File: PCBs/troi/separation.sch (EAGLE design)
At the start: 4 parts

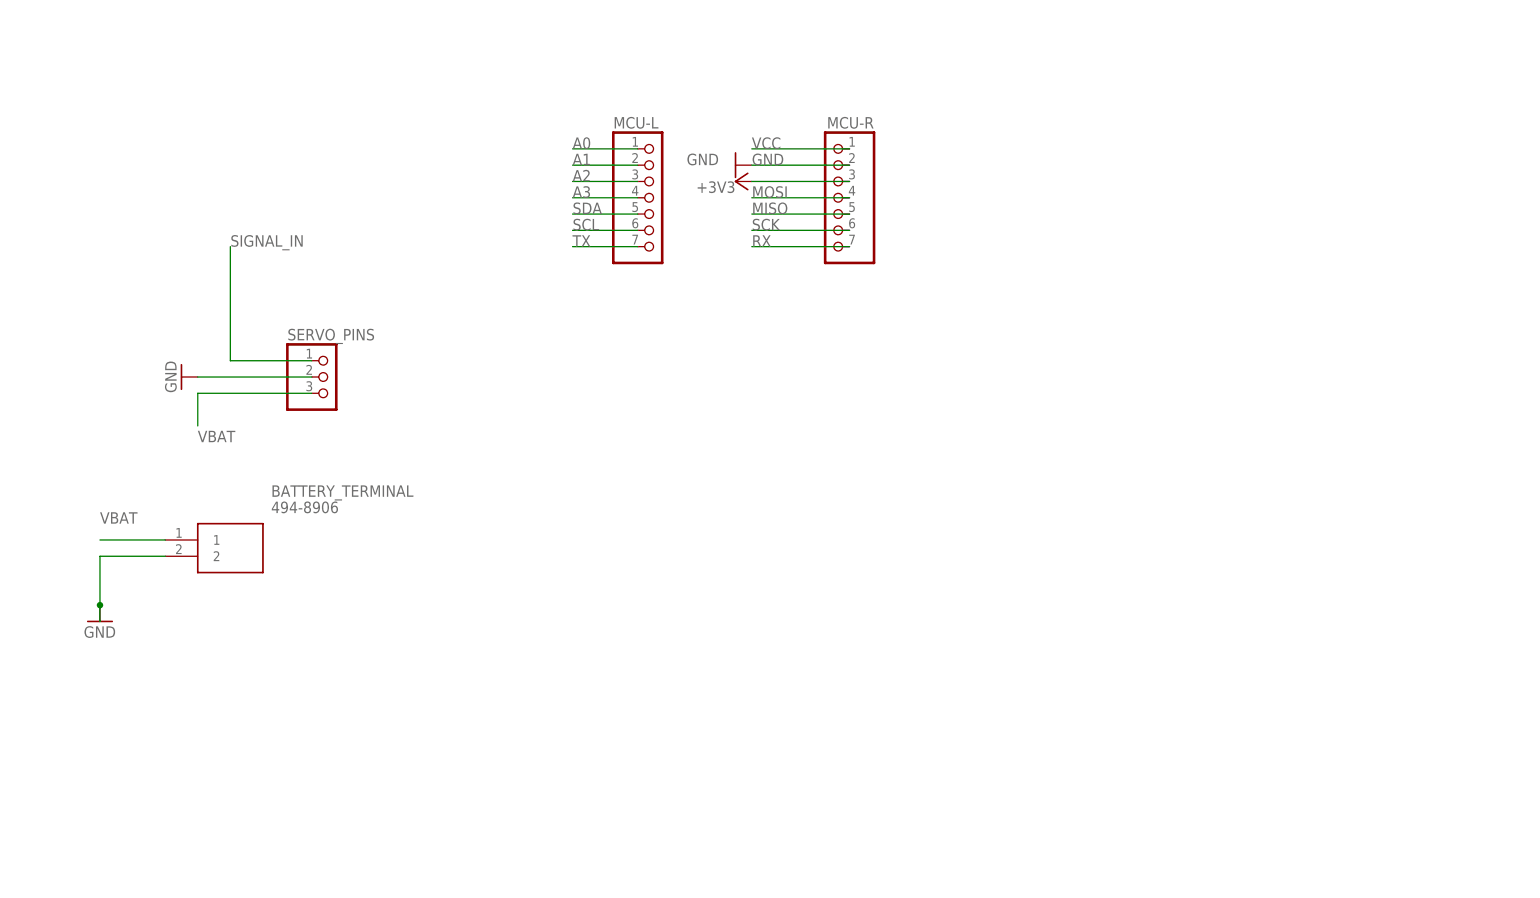
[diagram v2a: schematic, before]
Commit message: added mosfet transistor
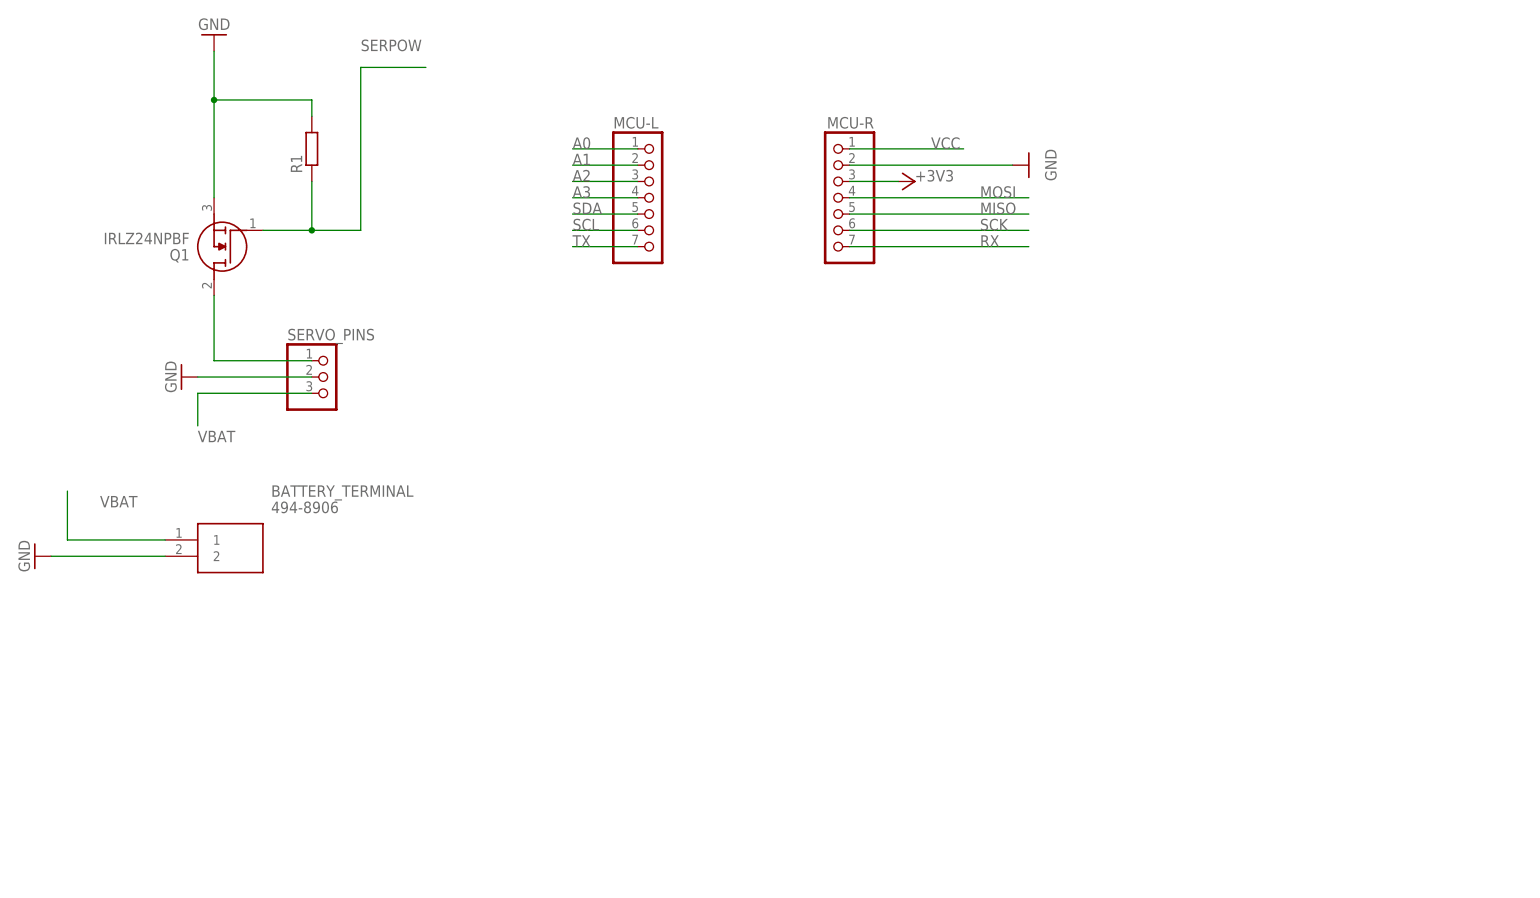
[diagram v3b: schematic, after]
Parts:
- added Q1: IRLZ24NPBF, SamacSys_Parts:IRLZ24NPBF
- added R1: (no value), rcl:R-EU_0204/7
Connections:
- removed net SIGNAL_IN: SERVO_PINS.1
- new net N$1: Q1.D, SERVO_PINS.1
- new net SERPOW: Q1.G, R1.1
- net GND: now also Q1.S, R1.2
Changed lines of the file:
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@@
 <part name="BATTERY_TERMINAL" library="494-8906" deviceset="494-8906" device=""/>
 <part name="GND3" library="supply1" library_urn="urn:adsk.eagle:library:371" deviceset="GND" device=""/>
+<part name="Q1" library="SamacSys_Parts" deviceset="IRLZ24NPBF" device=""/>
+<part name="GND4" library="supply1" library_urn="urn:adsk.eagle:library:371" deviceset="GND" device=""/>
+<part name="R1" library="rcl" library_urn="urn:adsk.eagle:library:334" deviceset="R-EU_" device="0204/7" package3d_urn="urn:adsk.eagle:package:23498/2"/>
 </parts>
 <sheets>
@@
 <attribute name="VALUE" x="115.57" y="68.58" size="1.778" layer="96" rot="MR0"/>
 </instance>
-<instance part="+3V1" gate="G$1" x="93.98" y="83.82" smashed="yes" rot="R90">
-<attribute name="VALUE" x="93.98" y="83.82" size="1.778" layer="96" rot="R180"/>
-</instance>
-<instance part="GND1" gate="1" x="93.98" y="86.36" smashed="yes" rot="R270">
-<attribute name="VALUE" x="86.36" y="86.36" size="1.778" layer="96"/>
+<instance part="+3V1" gate="G$1" x="121.92" y="83.82" smashed="yes" rot="R270">
+<attribute name="VALUE" x="121.92" y="83.82" size="1.778" layer="96"/>
+</instance>
+<instance part="GND1" gate="1" x="139.7" y="86.36" smashed="yes" rot="R90">
+<attribute name="VALUE" x="142.24" y="88.9" size="1.778" layer="96" rot="R270"/>
 </instance>
 <instance part="SERVO_PINS" gate="A" x="30.48" y="53.34" smashed="yes">
@@
 <attribute name="VALUE" x="21.59" y="33.02" size="1.778" layer="96" align="center-left"/>
 </instance>
-<instance part="GND3" gate="1" x="-5.08" y="15.24" smashed="yes">
-<attribute name="VALUE" x="-7.62" y="12.7" size="1.778" layer="96"/>
+<instance part="GND3" gate="1" x="-15.24" y="25.4" smashed="yes" rot="R270">
+<attribute name="VALUE" x="-17.78" y="27.94" size="1.778" layer="96" rot="R270"/>
+</instance>
+<instance part="Q1" gate="G$1" x="20.32" y="76.2" smashed="yes" rot="R180">
+<attribute name="NAME" x="8.89" y="72.39" size="1.778" layer="95" rot="R180" align="center-left"/>
+<attribute name="VALUE" x="8.89" y="74.93" size="1.778" layer="96" rot="R180" align="center-left"/>
+</instance>
+<instance part="GND4" gate="1" x="12.7" y="106.68" smashed="yes" rot="R180">
+<attribute name="VALUE" x="15.24" y="109.22" size="1.778" layer="96" rot="R180"/>
+</instance>
+<instance part="R1" gate="G$1" x="27.94" y="88.9" smashed="yes" rot="R90">
+<attribute name="NAME" x="26.4414" y="85.09" size="1.778" layer="95" rot="R90"/>
+<attribute name="VALUE" x="31.242" y="85.09" size="1.778" layer="96" rot="R90"/>
 </instance>
 </instances>
@@
 <segment>
 <pinref part="MCU-R" gate="A" pin="1"/>
-<wire x1="111.76" y1="88.9" x2="96.52" y2="88.9" width="0.1524" layer="91"/>
-<label x="96.52" y="88.9" size="1.778" layer="95"/>
+<wire x1="111.76" y1="88.9" x2="129.54" y2="88.9" width="0.1524" layer="91"/>
+<label x="124.46" y="88.9" size="1.778" layer="95"/>
 </segment>
 </net>
@@
 <segment>
 <pinref part="MCU-R" gate="A" pin="2"/>
-<wire x1="111.76" y1="86.36" x2="96.52" y2="86.36" width="0.1524" layer="91"/>
-<label x="96.52" y="86.36" size="1.778" layer="95"/>
+<wire x1="111.76" y1="86.36" x2="137.16" y2="86.36" width="0.1524" layer="91"/>
 <pinref part="GND1" gate="1" pin="GND"/>
 </segment>
@@
 <segment>
 <pinref part="BATTERY_TERMINAL" gate="G$1" pin="2"/>
-<wire x1="5.08" y1="25.4" x2="-5.08" y2="25.4" width="0.1524" layer="91"/>
-<wire x1="-5.08" y1="25.4" x2="-5.08" y2="17.78" width="0.1524" layer="91"/>
 <pinref part="GND3" gate="1" pin="GND"/>
-<wire x1="-5.08" y1="17.78" x2="-5.08" y2="15.24" width="0.1524" layer="91"/>
-<junction x="-5.08" y="17.78"/>
+<wire x1="5.08" y1="25.4" x2="-12.7" y2="25.4" width="0.1524" layer="91"/>
+</segment>
+<segment>
+<pinref part="Q1" gate="G$1" pin="S"/>
+<wire x1="12.7" y1="81.28" x2="12.7" y2="96.52" width="0.1524" layer="91"/>
+<wire x1="12.7" y1="96.52" x2="12.7" y2="104.14" width="0.1524" layer="91"/>
+<pinref part="GND4" gate="1" pin="GND"/>
+<pinref part="R1" gate="G$1" pin="2"/>
+<wire x1="27.94" y1="93.98" x2="27.94" y2="96.52" width="0.1524" layer="91"/>
+<wire x1="27.94" y1="96.52" x2="12.7" y2="96.52" width="0.1524" layer="91"/>
+<junction x="12.7" y="96.52"/>
 </segment>
 </net>
@@
 <segment>
 <pinref part="MCU-R" gate="A" pin="3"/>
-<wire x1="111.76" y1="83.82" x2="96.52" y2="83.82" width="0.1524" layer="91"/>
+<wire x1="111.76" y1="83.82" x2="119.38" y2="83.82" width="0.1524" layer="91"/>
 <pinref part="+3V1" gate="G$1" pin="+3V3"/>
 </segment>
@@
 <segment>
 <pinref part="MCU-R" gate="A" pin="4"/>
-<wire x1="111.76" y1="81.28" x2="96.52" y2="81.28" width="0.1524" layer="91"/>
-<label x="96.52" y="81.28" size="1.778" layer="95"/>
+<wire x1="111.76" y1="81.28" x2="139.7" y2="81.28" width="0.1524" layer="91"/>
+<label x="132.08" y="81.28" size="1.778" layer="95"/>
 </segment>
 </net>
@@
 <segment>
 <pinref part="MCU-R" gate="A" pin="5"/>
-<wire x1="111.76" y1="78.74" x2="96.52" y2="78.74" width="0.1524" layer="91"/>
-<label x="96.52" y="78.74" size="1.778" layer="95"/>
+<wire x1="111.76" y1="78.74" x2="139.7" y2="78.74" width="0.1524" layer="91"/>
+<label x="132.08" y="78.74" size="1.778" layer="95"/>
 </segment>
 </net>
@@
 <segment>
 <pinref part="MCU-R" gate="A" pin="6"/>
-<wire x1="111.76" y1="76.2" x2="96.52" y2="76.2" width="0.1524" layer="91"/>
-<label x="96.52" y="76.2" size="1.778" layer="95"/>
+<wire x1="111.76" y1="76.2" x2="139.7" y2="76.2" width="0.1524" layer="91"/>
+<label x="132.08" y="76.2" size="1.778" layer="95"/>
 </segment>
 </net>
@@
 <segment>
 <pinref part="MCU-R" gate="A" pin="7"/>
-<wire x1="111.76" y1="73.66" x2="96.52" y2="73.66" width="0.1524" layer="91"/>
-<label x="96.52" y="73.66" size="1.778" layer="95"/>
-</segment>
-</net>
-<net name="SIGNAL_IN" class="0">
-<segment>
-<pinref part="SERVO_PINS" gate="A" pin="1"/>
-<wire x1="27.94" y1="55.88" x2="15.24" y2="55.88" width="0.1524" layer="91"/>
-<wire x1="15.24" y1="55.88" x2="15.24" y2="73.66" width="0.1524" layer="91"/>
-<label x="15.24" y="73.66" size="1.778" layer="95"/>
+<wire x1="111.76" y1="73.66" x2="139.7" y2="73.66" width="0.1524" layer="91"/>
+<label x="132.08" y="73.66" size="1.778" layer="95"/>
 </segment>
 </net>
@@
 <segment>
 <pinref part="BATTERY_TERMINAL" gate="G$1" pin="1"/>
-<wire x1="5.08" y1="27.94" x2="-5.08" y2="27.94" width="0.1524" layer="91"/>
-<label x="-5.08" y="30.48" size="1.778" layer="95"/>
+<wire x1="5.08" y1="27.94" x2="-10.16" y2="27.94" width="0.1524" layer="91"/>
+<label x="-5.08" y="33.02" size="1.778" layer="95"/>
+<wire x1="-10.16" y1="27.94" x2="-10.16" y2="35.56" width="0.1524" layer="91"/>
+</segment>
+</net>
+<net name="N$1" class="0">
+<segment>
+<pinref part="SERVO_PINS" gate="A" pin="1"/>
+<wire x1="27.94" y1="55.88" x2="12.7" y2="55.88" width="0.1524" layer="91"/>
+<pinref part="Q1" gate="G$1" pin="D"/>
+<wire x1="12.7" y1="55.88" x2="12.7" y2="66.04" width="0.1524" layer="91"/>
+</segment>
+</net>
+<net name="SERPOW" class="0">
+<segment>
+<pinref part="Q1" gate="G$1" pin="G"/>
+<wire x1="20.32" y1="76.2" x2="27.94" y2="76.2" width="0.1524" layer="91"/>
+<wire x1="27.94" y1="76.2" x2="35.56" y2="76.2" width="0.1524" layer="91"/>
+<wire x1="35.56" y1="76.2" x2="35.56" y2="101.6" width="0.1524" layer="91"/>
+<wire x1="35.56" y1="101.6" x2="45.72" y2="101.6" width="0.1524" layer="91"/>
+<wire x1="27.94" y1="76.2" x2="27.94" y2="83.82" width="0.1524" layer="91"/>
+<junction x="27.94" y="76.2"/>
+<pinref part="R1" gate="G$1" pin="1"/>
+<label x="35.56" y="104.14" size="1.778" layer="95"/>
 </segment>
 </net>
@@
 packages will not be understood (or retained) with this version.
 </note>
+<note version="8.4" severity="warning">
+Since Version 8.4, EAGLE supports properties for SPICE simulation.
+Probes in schematics and SPICE mapping objects found in parts and library devices
+will not be understood with this version. Update EAGLE to the latest version
+for full support of SPICE simulation.
+</note>
 </compatibility>

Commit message: complete rest of separation schematic
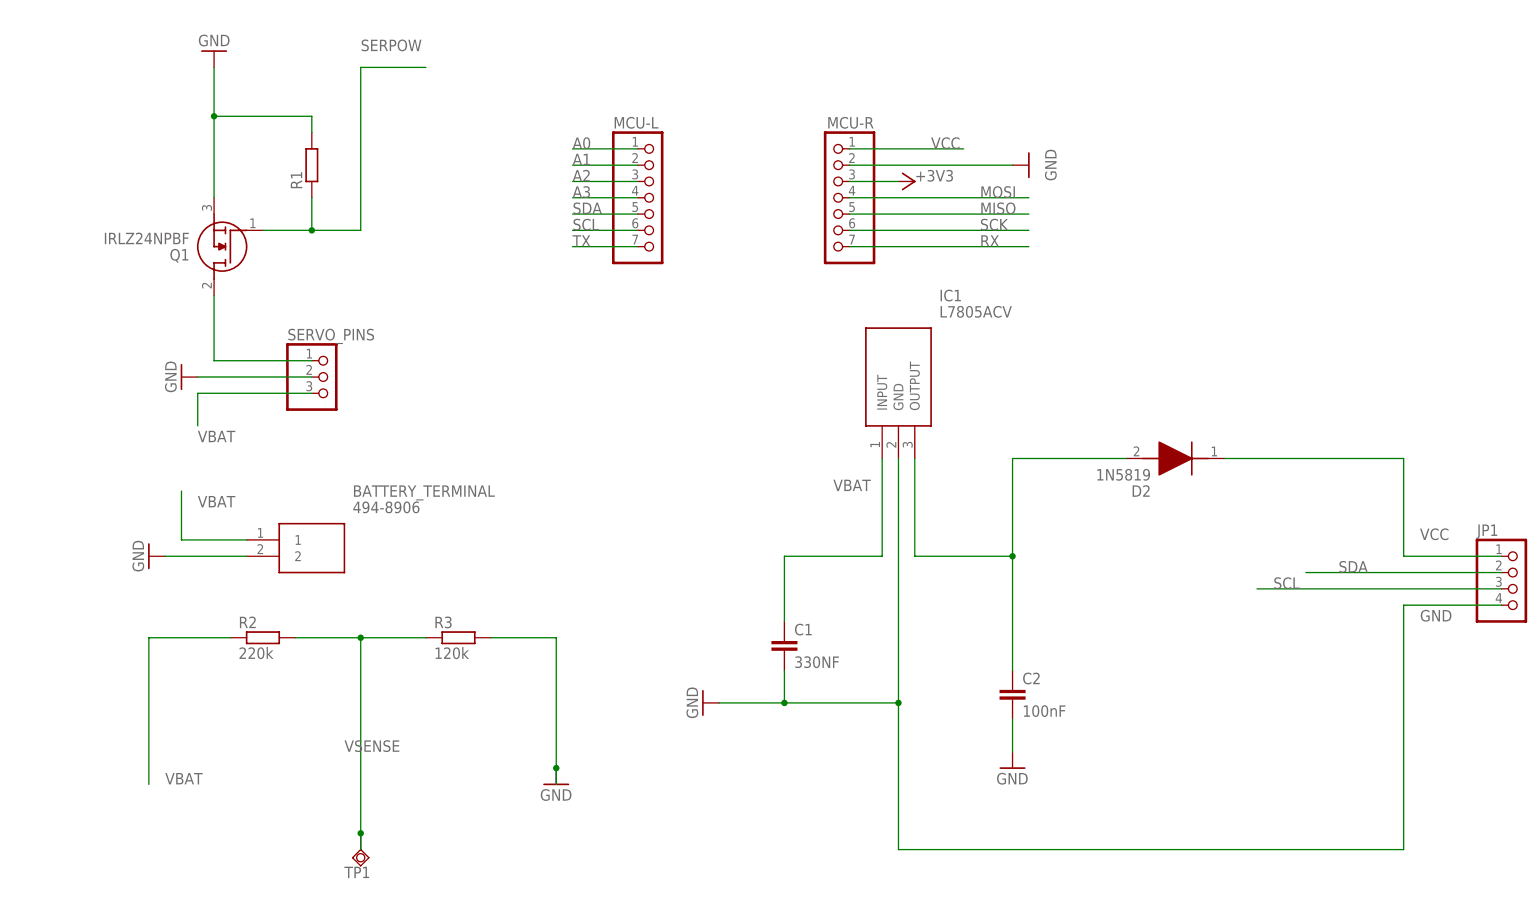
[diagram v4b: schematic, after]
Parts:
- added C1: 330NF, capacitor-wima:C2,5-3
- added C2: 100nF, capacitor-wima:C2,5-3
- added D2: 1N5819, SamacSys_Parts:1N5819
- added IC1: L7805ACV, SamacSys_Parts:L7805ACV
- added JP1: (no value), pinhead:PINHD-1X4
- added R2: 220k, rcl:R-EU_0204/7
- added R3: 120k, rcl:R-EU_0204/7
- added TP1: TPSQB1,27, testpad:TPSQB1,27
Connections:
- new net N$4: C2.1, D2.A, IC1.OUTPUT
- new net VSENSE: R2.2, R3.1, TP1.TP
- net GND: now also C1.2, C2.2, IC1.GND, JP1.4, R3.2
- net SCL: now also JP1.3
- net SDA: now also JP1.2
- net VBAT: now also C1.1, IC1.INPUT, R2.1
- net VCC: now also D2.K, JP1.1
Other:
- moved on the sheet: BATTERY_TERMINAL, R1
